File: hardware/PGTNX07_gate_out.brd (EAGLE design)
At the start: 111.7 x 77.5 mm, 109 parts, among them IC1 74HC595N, IC10 74HC595N, IC11 TL074P, IC12 TL074P, IC2 TL074P, IC3 TL074P, IC4 74HC595N, IC5 TL074P, IC6 TL074P, IC7 74HC595N, IC8 TL074P, IC9 TL074P

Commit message: Tidy up scheamtics
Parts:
- added CLOCK2, LATCH2: HEADER/MALE/01, connectors:HEADER/MALE/01
- moved DIN 7.62 mm to (14.0, 77.5)
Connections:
- net CLK2 renamed +5V
- net N$19: now also CLOCK2.1
- net N$33: now also LATCH2.1
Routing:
- net N$19: track 124.3 -> 272.8 mm, vias 2 -> 3
- net N$33: track 108.8 -> 146.9 mm, vias 5 -> 7
- net N$4: track 16.6 -> 25.4 mm
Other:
- board text added: "INPUTS"
- board text added: "OUTPUTS"

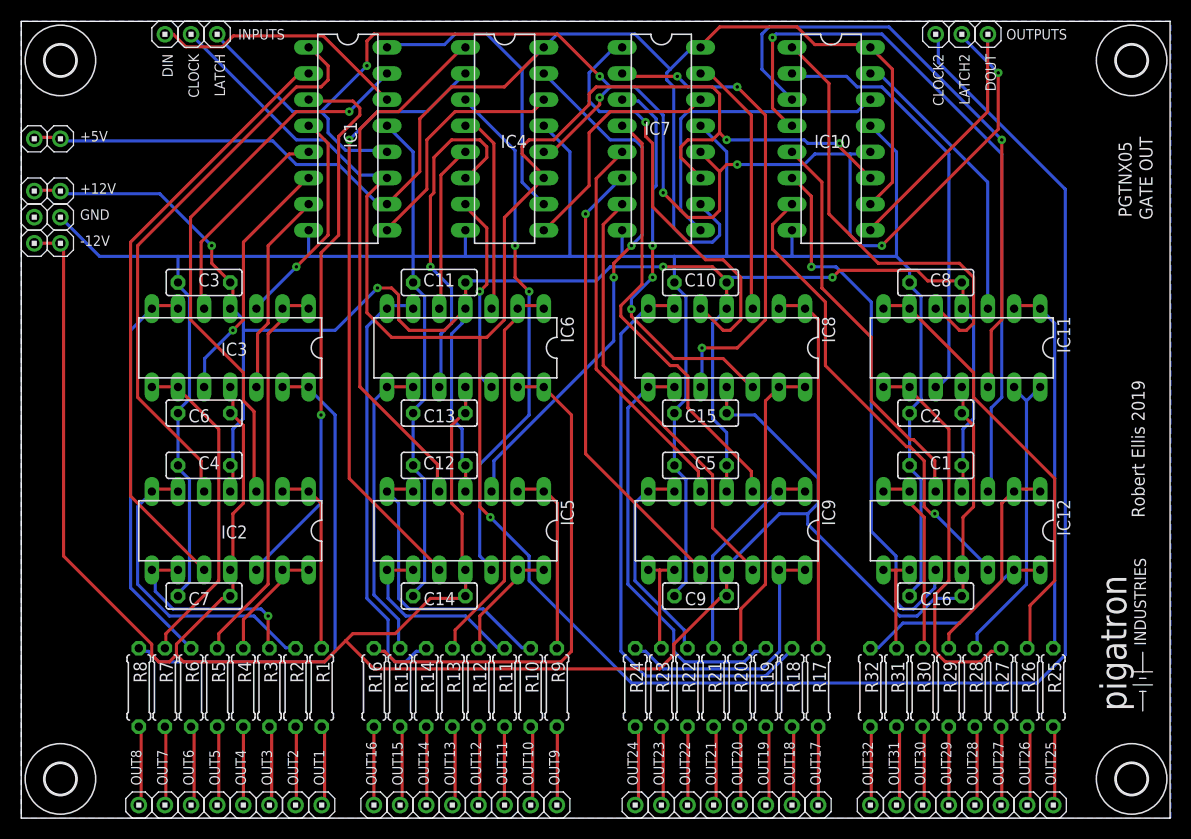
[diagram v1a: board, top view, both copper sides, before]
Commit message: Added seperate headers for driving leds from outputs
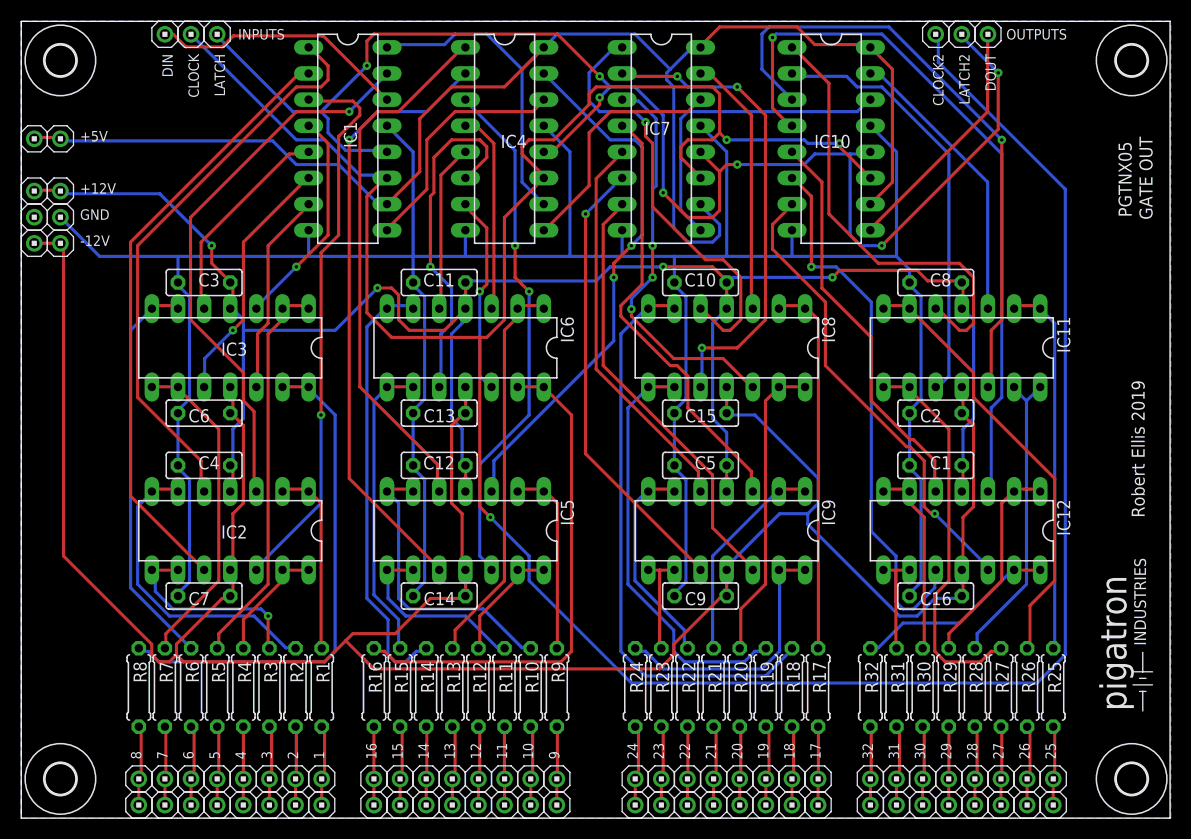
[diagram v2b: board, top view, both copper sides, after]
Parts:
- added 1, 10, 11, 12, 13, 14, 15, 16, 17, 18, 19, 2, 20, 21, 22, 23, 24, 25, 26, 27, 28, 29, 3, 30, 31, 32, 4, 5, 6, 7, 8, 9: HEADER/MALE/01, connectors:HEADER/MALE/01
- turned LED1 to 0 degrees
- turned LED10 to 0 degrees
- turned LED11 to 0 degrees
- turned LED12 to 0 degrees
- turned LED13 to 0 degrees
- turned LED14 to 0 degrees
- turned LED15 to 0 degrees
- turned LED16 to 0 degrees
- turned LED17 to 0 degrees
- turned LED18 to 0 degrees
- turned LED19 to 0 degrees
- turned LED2 to 0 degrees
- turned LED20 to 0 degrees
- turned LED21 to 0 degrees
- turned LED22 to 0 degrees
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- renumbered OUT1 to LED1, OUT10 to LED10, OUT11 to LED11, OUT12 to LED12, OUT13 to LED13, OUT14 to LED14, OUT15 to LED15, OUT16 to LED16, OUT17 to LED17, OUT18 to LED18, OUT19 to LED19, OUT2 to LED2, OUT20 to LED20, OUT21 to LED21, OUT22 to LED22, OUT23 to LED23, OUT24 to LED24, OUT25 to LED25, OUT26 to LED26, OUT27 to LED27, OUT28 to LED28, OUT29 to LED29, OUT3 to LED3, OUT30 to LED30, OUT31 to LED31, OUT32 to LED32, OUT4 to LED4, OUT5 to LED5, OUT6 to LED6, OUT7 to LED7, OUT8 to LED8, OUT9 to LED9
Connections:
- net N$103: now also 27.1
- net N$104: now also 28.1
- net N$105: now also 29.1
- net N$106: now also 30.1
- net N$107: now also 31.1
- net N$108: now also 32.1
- net N$14: now also 1.1
- net N$16: now also 2.1
- net N$27: now also 3.1
- net N$28: now also 4.1
- net N$29: now also 5.1
- net N$30: now also 6.1
- net N$31: now also 7.1
- net N$32: now also 8.1
- net N$44: now also 9.1
- net N$46: now also 10.1
- net N$55: now also 11.1
- net N$56: now also 12.1
- net N$57: now also 13.1
- net N$58: now also 14.1
- net N$59: now also 15.1
- net N$60: now also 16.1
- net N$69: now also 17.1
- net N$71: now also 18.1
- net N$78: now also 19.1
- net N$79: now also 20.1
- net N$80: now also 21.1
- net N$81: now also 22.1
- net N$82: now also 23.1
- net N$83: now also 24.1
- net N$94: now also 25.1
- net N$96: now also 26.1
